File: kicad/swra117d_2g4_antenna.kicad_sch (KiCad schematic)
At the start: 2 parts, among them J1 SMA edge launch

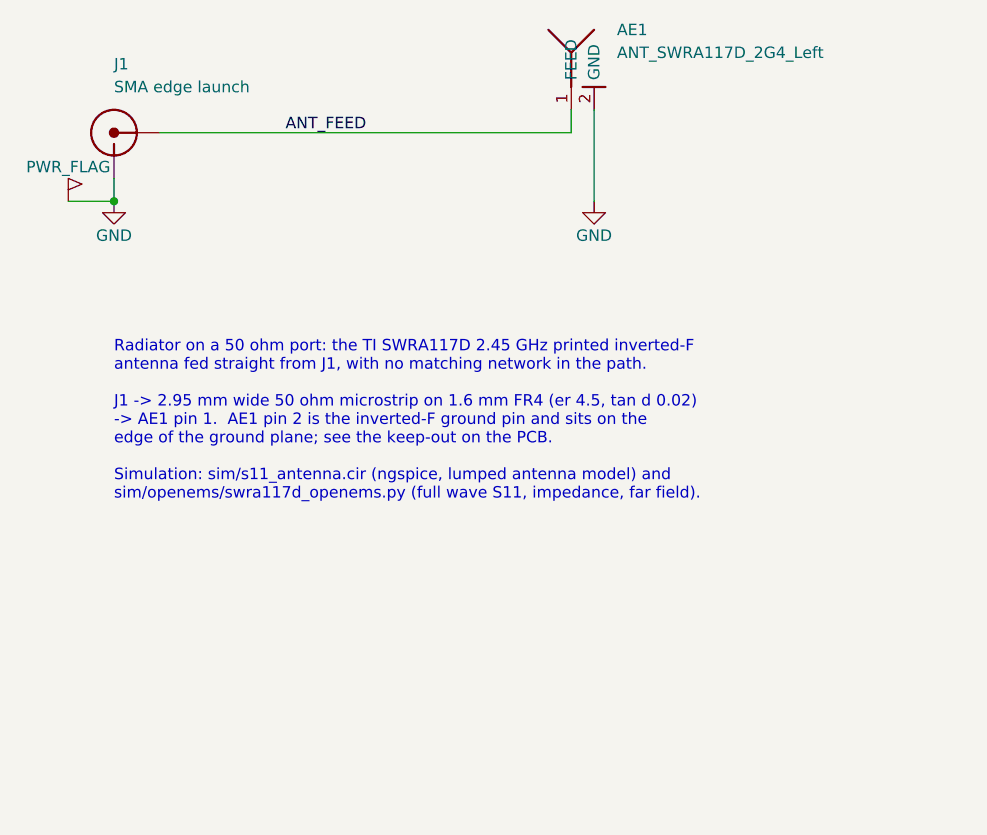
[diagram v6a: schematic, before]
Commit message: Pi network on the first board: pads, and a 0 ohm link
Asked for the matching components, with the condition "if 50 ohm matching is
mandatory".  It is not mandatory as values and there are none to fit:
SWRA117D says the antenna is already a 50 ohm design and publishes no matching
BOM.  Inventing an L and a C would repeat the 0.8 nH this project already got
wrong once by fitting it to its own model.

What AN058 section 3.4 actually asks for is the network to exist: "If the
antenna design is adequately matched then it just takes one zero ohm resistor
or DC block cap to be inserted into the pi-matching network."  So that is what
is fitted:

  Z2  0R     series - the link.  100 pF is the drop-in where the radio needs
             DC isolation, which this antenna's DC short to ground makes worth
             checking
  Z1  DNP    shunt, connector side
  Z3  DNP    shunt, antenna side

Z1 and Z3 exist because AN058's own measurements show an enclosure only ever
pulls resonance down, and a board with nowhere to compensate gets respun.

Three problems the checkers found on the way, all real:

  * A 2.95 mm track cannot butt onto an 0402 land.  KiCad tracks are
    round-capped, so the cap bulges 1.475 mm past the endpoint and lands
    across the opposite pad, 0.96 mm away - KiCad's own DRC would have said
    so too.  Necking the line down is worse: 0.6 mm is ~100 ohm here and the
    6.5 mm to taper down and back is 3.8 nH, j58 ohm at 2.45 GHz, in series
    with the antenna.  So the series land is widened to the line instead
    (Chip_0402_RF_WideLand: 0402 pitch, 2.95 mm pads) and the wide line stops
    2.0 mm short so its cap reaches into its own pad and clears the other.
    The shunts keep the ordinary land on a 0.6 mm stub, which is not in the
    through path.
  * check_feed_width had been taking the last non-GND pad it saw as the port,
    which the new 0402s took over.  It now looks for the footprint that brings
    its own B.Cu reference copper - which is what a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
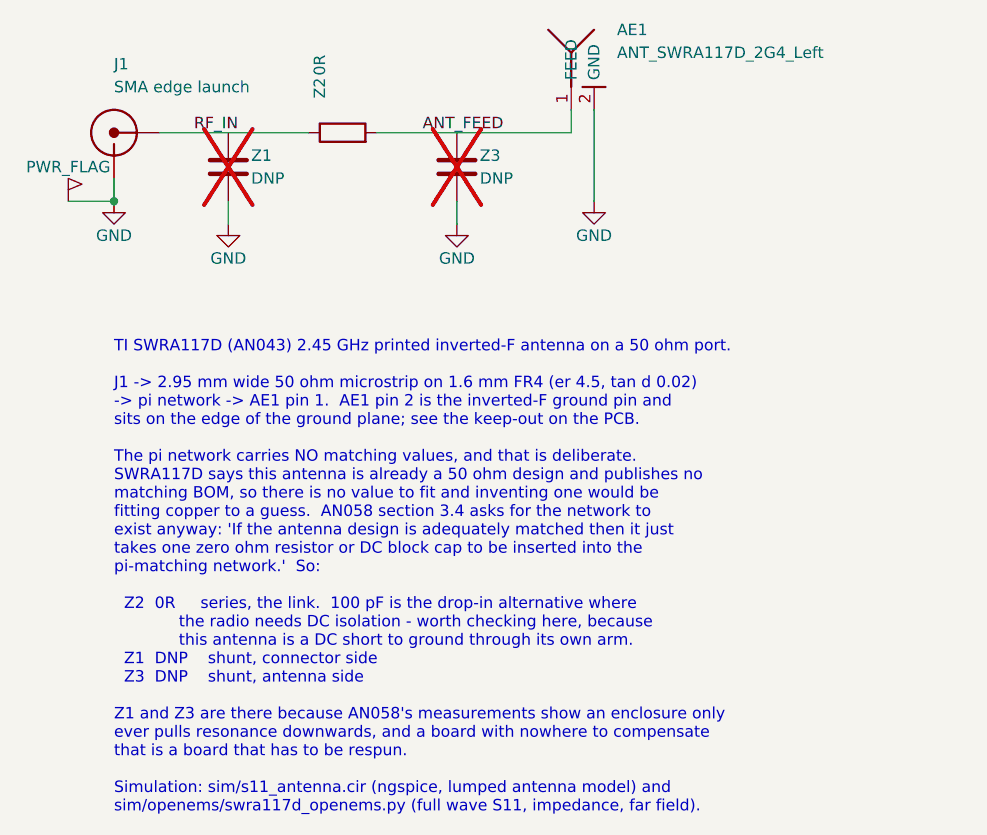
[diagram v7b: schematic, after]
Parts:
- added Z1, Z3: DNP, SWRA117D_RF:Chip_0402_1005Metric_RF, symbol SWRA117D_RF:C
- added Z2: 0R, SWRA117D_RF:Chip_0402_RF_WideLand, symbol SWRA117D_RF:R
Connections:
- net ANT_FEED: now also Z2.2; no longer J1.1 (In)
- net GND: now also Z1.2, Z3.2
- new net RF_IN: J1.1 (In), Z2.1
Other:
- note added: "TI SWRA117D (AN043) 2.45 GHz printed inverted-F antenna on a 50 ohm port. J1 -> 2.95 mm wide 50 ohm microstrip on 1.6 mm FR4 (er 4.5, tan d 0.02) -> pi network -> AE1 pin 1. AE1 pin 2 is the inverted-F ground pin and sits on the edge of the ground plane; see the keep-out on the PCB. The pi network carries NO matching values, and that is deliberate. SWRA117D says this antenna is already a 50 ohm d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"
- note removed: "Radiator on a 50 ohm port: the TI SWRA117D 2.45 GHz printed inverted-F antenna fed straight from J1, with no matching network in the path. J1 -> 2.95 mm wide 50 ohm microstrip on 1.6 mm FR4 (er 4.5, tan d 0.02) -> AE1 pin 1. AE1 pin 2 is the inverted-F ground pin and sits on the edge of the ground plane; see the keep-out on the PCB. Simulation: sim/s11_antenna.cir (ngspice, lumped antenna model) 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"
- title: 2.45 GHz PCB antenna (TI SWRA117D) - radiator on a 50 ohm SMA port -> 2.45 GHz PCB antenna (TI SWRA117D/AN043) - radiator on a 50 ohm SMA port, pi network fitted as a 0 ohm link
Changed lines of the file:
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@@
 	(paper "A4")
 	(title_block
-		(title "2.45 GHz PCB antenna (TI SWRA117D) - radiator on a 50 ohm SMA port")
+		(title "2.45 GHz PCB antenna (TI SWRA117D/AN043) - radiator on a 50 ohm SMA port, pi network fitted as a 0 ohm link"
+		)
 		(date "2026-09-12")
 		(rev "A")
-		(comment 1 "Radiator fed straight from the SMA port, no matching network")
+		(comment 1 "Pi network laid out, fitted as a 0 ohm link: no matching values are published for this antenna"
+		)
 		(comment 2 "Antenna keep-out: no copper on any layer")
 	)
 	(wire
-		(pts (xy 81.28 88.9) (xy 127 88.9))
+		(pts (xy 81.28 88.9) (xy 97.79 88.9))
+		(stroke (width 0) (type default))
+	)
+	(wire
+		(pts (xy 105.41 88.9) (xy 127 88.9))
 		(stroke (width 0) (type default))
 	)
@@
 	(wire
 		(pts (xy 76.2 96.52) (xy 71.12 96.52))
+		(stroke (width 0) (type default))
+	)
+	(wire
+		(pts (xy 88.9 96.52) (xy 88.9 99.06))
+		(stroke (width 0) (type default))
+	)
+	(wire
+		(pts (xy 114.3 96.52) (xy 114.3 99.06))
 		(stroke (width 0) (type default))
 	)
@@
 		(color 0 0 0 0)
 	)
+	(label "RF_IN"
+		(at 85.09 88.9 0)
+		(effects (font (size 1.27 1.27)) (justify left bottom))
+	)
 	(label "ANT_FEED"
-		(at 95.25 88.9 0)
+		(at 110.49 88.9 0)
 		(effects (font (size 1.27 1.27)) (justify left bottom))
 	)
-	(text "Radiator on a 50 ohm port: the TI SWRA117D 2.45 GHz printed inverted-F\nantenna fed straight from J1, with no matching network in the path.\n\nJ1 -> 2.95 mm wide 50 ohm microstrip on 1.6 mm FR4 (er 4.5, tan d 0.02)\n-> AE1 pin 1.  AE1 pin 2 is the inverted-F ground pin and sits on the\nedge of the ground plane; see the keep-out on the PCB.\n\nSimulation: sim/s11_antenna.cir (ngspice, lumped antenna model) and\nsim/openems/swra117d_openems.py (full wave S11, impedance, far field)."
+	(text "TI SWRA117D (AN043) 2.45 GHz printed inverted-F antenna on a 50 ohm port.\n\nJ1 -> 2.95 mm wide 50 ohm microstrip on 1.6 mm FR4 (er 4.5, tan d 0.02)\n-> pi network -> AE1 pin 1.  AE1 pin 2 is the inverted-F ground pin and\nsits on the edge of the ground plane; see the keep-out on the PCB.\n\nThe pi network carries NO matching values, and that is deliberate.\nSWRA117D says this antenna is already a 50 ohm design and publishes no\nmatching BOM, so there is no value to fit and inventing one would be\nfitting copper to a guess.  AN058 section 3.4 asks for the network to\nexist anyway: 'If the antenna design is adequately matched then it just\ntakes one zero ohm resistor or DC block cap to be inserted into the\npi-matching network.'  So:\n\n  Z2  0R     series, the link.  100 pF is the drop-in alternative where\n             the radio needs DC isolation - worth checking here, because\n             this antenna is a DC short to ground through its own arm.\n  Z1  DNP    shunt, connector side\n  Z3  DNP    shunt, antenna side\n\nZ1 and Z3 are there because AN058's measurements show an enclosure only\never pulls resonance downwards, and a board with nowhere to compensate\nthat is a board that has to be respun.\n\nSimulation: sim/s11_antenna.cir (ngspice, lumped antenna model) and\nsim/openems/swra117d_openems.py (full wave S11, impedance, far field)."
 		(exclude_from_sim no)
 		(at 76.2 112 0)
@@
 			(project "swra117d_2g4_antenna"
 				(path "/0c52b35a-5623-5f55-988d-762afc65fb88" (reference "J1") (unit 1))
+			)
+		)
+	)
+	(symbol
+		(lib_id "SWRA117D_RF:C")
+		(at 88.9 92.71 0)
+		(unit 1)
+		(exclude_from_sim no)
+		(in_bom no)
+		(on_board yes)
+		(dnp yes)
+		(property "Reference" "Z1"
+			(at 91.44 91.44 0)
+			(effects (font (size 1.27 1.27)) (justify left))
+		)
+		(property "Value" "DNP" (at 91.44 93.98 0) (effects (font (size 1.27 1.27)) (justify left)))
+		(property "Footprint" "SWRA117D_RF:Chip_0402_1005Metric_RF"
+			(at 88.9 92.71 0)
+			(effects (font (size 1.27 1.27)) (hide yes))
+		)
+		(property "Datasheet" "~" (at 88.9 92.71 0) (effects (font (size 1.27 1.27)) (hide yes)))
+		(property "Description" "Pi network, shunt on the connector side. Not fitted: SWRA117D publishes no matching values for this antenna. Laid out because AN058 asks for somewhere to compensate an enclosure"
+			(at 88.9 92.71 0)
+			(effects (font (size 1.27 1.27)) (hide yes))
+		)
+		(pin "1")
+		(pin "2")
+		(instances
+			(project "swra117d_2g4_antenna"
+				(path "/0c52b35a-5623-5f55-988d-762afc65fb88" (reference "Z1") (unit 1))
+			)
+		)
+	)
+	(symbol
+		(lib_id "SWRA117D_RF:R")
+		(at 101.6 88.9 90)
+		(unit 1)
+		(exclude_from_sim no)
+		(in_bom yes)
+		(on_board yes)
+		(dnp no)
+		(property "Reference" "Z2"
+			(at 99.06 85.09 0)
+			(effects (font (size 1.27 1.27)) (justify left))
+		)
+		(property "Value" "0R" (at 99.06 82.55 0) (effects (font (size 1.27 1.27)) (justify left)))
+		(property "Footprint" "SWRA117D_RF:Chip_0402_RF_WideLand"
+			(at 101.6 88.9 0)
+			(effects (font (size 1.27 1.27)) (hide yes))
+		)
+		(property "Datasheet" "~" (at 101.6 88.9 0) (effects (font (size 1.27 1.27)) (hide yes)))
+		(property "Description" "Pi network, series. 0 ohm link: AN058 section 3.4 - an already matched antenna 'just takes one zero ohm resistor or DC block cap'. A 100 pF is the drop-in alternative where the radio needs DC isolation, which this antenna's DC short to ground makes worth checking"
+			(at 101.6 88.9 0)
+			(effects (font (size 1.27 1.27)) (hide yes))
+		)
+		(pin "1")
+		(pin "2")
+		(instances
+			(project "swra117d_2g4_antenna"
+				(path "/0c52b35a-5623-5f55-988d-762afc65fb88" (reference "Z2") (unit 1))
+			)
+		)
+	)
+	(symbol
+		(lib_id "SWRA117D_RF:C")
+		(at 114.3 92.71 0)
+		(unit 1)
+		(exclude_from_sim no)
+		(in_bom no)
+		(on_board yes)
+		(dnp yes)
+		(property "Reference" "Z3"
+			(at 116.84 91.44 0)
+			(effects (font (size 1.27 1.27)) (justify left))
+		)
+		(property "Value" "DNP" (at 116.84 93.98 0) (effects (font (size 1.27 1.27)) (justify left)))
+		(property "Footprint" "SWRA117D_RF:Chip_0402_1005Metric_RF"
+			(at 114.3 92.71 0)
+			(effects (font (size 1.27 1.27)) (hide yes))
+		)
+		(property "Datasheet" "~" (at 114.3 92.71 0) (effects (font (size 1.27 1.27)) (hide yes)))
+		(property "Description" "Pi network, shunt on the antenna side. Not fitted, same reason as Z1"
+			(at 114.3 92.71 0)
+			(effects (font (size 1.27 1.27)) (hide yes))
+		)
+		(pin "1")
+		(pin "2")
+		(instances
+			(project "swra117d_2g4_antenna"
+				(path "/0c52b35a-5623-5f55-988d-762afc65fb88" (reference "Z3") (unit 1))
 			)
 		)
@@
 			)
 		)
+	)
+	(symbol
+		(lib_id "SWRA117D_RF:GND")
+		(at 88.9 99.06 0)
+		(unit 1)
+		(exclude_from_sim no)
+		(in_bom yes)
+		(on_board yes)
+		(dnp no)
+		(property "Reference" "#PWR03"
+			(at 88.9 105.41 0)
+			(effects (font (size 1.27 1.27)) (hide yes))
+		)
+		(property "Value" "GND" (at 88.9 102.87 0) (effects (font (size 1.27 1.27))))
+		(property "Footprint" "" (at 88.9 99.06 0) (effects (font (size 1.27 1.27)) (hide yes)))
+		(property "Datasheet" "" (at 88.9 99.06 0) (effects (font (size 1.27 1.27)) (hide yes)))
+		(property "Description" "Ground reference"
+			(at 88.9 99.06 0)
+			(effects (font (size 1.27 1.27)) (hide yes))
+		)
+		(pin "1")
+		(instances
+			(project "swra117d_2g4_antenna"
+				(path "/0c52b35a-5623-5f55-988d-762afc65fb88" (reference "#PWR03") (unit 1))
+			)
+		)
+	)
+	(symbol
+		(lib_id "SWRA117D_RF:GND")
+		(at 114.3 99.06 0)
+		(unit 1)
+		(exclude_from_sim no)
+		(in_bom yes)
+		(on_board yes)
+		(dnp no)
+		(property "Reference" "#PWR04"
+			(at 114.3 105.41 0)
+			(effects (font (size 1.27 1.27)) (hide yes))
+		)
+		(property "Value" "GND" (at 114.3 102.87 0) (effects (font (size 1.27 1.27))))
+		(property "Footprint" "" (at 114.3 99.06 0) (effects (font (size 1.27 1.27)) (hide yes)))
+		(property "Datasheet" "" (at 114.3 99.06 0) (effects (font (size 1.27 1.27)) (hide yes)))
+		(property "Description" "Ground reference"
+			(at 114.3 99.06 0)
+			(effects (font (size 1.27 1.27)) (hide yes))
+		)
+		(pin "1")
+		(instances
+			(project "swra117d_2g4_antenna"
+				(path "/0c52b35a-5623-5f55-988d-762afc65fb88" (reference "#PWR04") (unit 1))
+			)
+		)
